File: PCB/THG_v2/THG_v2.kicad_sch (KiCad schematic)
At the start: 9 parts, among them J1 AM2315_Conn, J2 Conn_01x04_Male, J3 Conn_01x04_Male, J4 Conn_01x06_Male, J5 Screw_Terminal_01x02, U1 mini_esp32

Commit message: adding previous gerber file
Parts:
- added R3: n/a, Resistor_THT:R_Axial_DIN0207_L6.3mm_D2.5mm_P10.16mm_Horizontal, symbol Device:R
- added S1: DTS-6, Lib_Kicad:DTS-6, symbol DTS-6:DTS-6
- J2: value Conn_01x04_Male -> LCD_conn
- J3: value Conn_01x04_Male -> RTC_Conn
- J4: value Conn_01x06_Male -> SD_card_conn
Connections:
- net +5V: now also S1.3
- net GND: now also U1.1 (GND), U1.22 (GND), U1.33 (GND), R3.1, S1.2
- new net: R3.2, S1.1

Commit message: adding pcb pic
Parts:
- J5: value Screw_Terminal_01x02 -> AC_in_terminal
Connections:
- net +5V: now also R1.1, R2.1
- net SCL: now also J1.4 (Pin_4)
- net SDA: now also J1.3 (Pin_3)
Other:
- moved on the sheet: J5, R1, R2

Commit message: rev
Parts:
- removed J1: AM2315_Conn, Connector_JST:JST_EH_B4B-EH-A_1x04_P2.50mm_Vertical, symbol Connector:Conn_01x04_Male
- added J1: AM2315_Jack, Lib_Kicad:TRRS-PJ-320A, symbol Connector:AudioJack3_Ground
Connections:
- net +5V: now also J1.T
- net GND: now also J1.G
- net SCL: now also J1.S
- net SDA: now also J1.R
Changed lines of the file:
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@@
-    (stroke (width 0) (type default) (color 0 0 0 0))
-  )
-  (wire (pts (xy 95.25 138.43) (xy 95.25 128.27))
-    (stroke (width 0) (type default) (color 0 0 0 0))
-  )
-  (wire (pts (xy 95.25 121.92) (xy 95.25 125.73))
     (stroke (width 0) (type default) (color 0 0 0 0))
   )
@@
     (stroke (width 0) (type default) (color 0 0 0 0))
   )
+  (wire (pts (xy 86.36 128.27) (xy 99.06 128.27))
+    (stroke (width 0) (type default) (color 0 0 0 0))
+  )
   (wire (pts (xy 215.9 129.54) (xy 212.09 129.54))
     (stroke (width 0) (type default) (color 0 0 0 0))
   )
-  (wire (pts (xy 74.93 133.35) (xy 72.39 133.35))
+  (wire (pts (xy 88.9 123.19) (xy 86.36 123.19))
     (stroke (width 0) (type default) (color 0 0 0 0))
   )
@@
     (stroke (width 0) (type default) (color 0 0 0 0))
   )
-  (wire (pts (xy 74.93 130.81) (xy 72.39 130.81))
+  (wire (pts (xy 88.9 125.73) (xy 86.36 125.73))
     (stroke (width 0) (type default) (color 0 0 0 0))
   )
@@
     (stroke (width 0) (type default) (color 0 0 0 0))
   )
-  (wire (pts (xy 95.25 128.27) (xy 72.39 128.27))
-    (stroke (width 0) (type default) (color 0 0 0 0))
-  )
   (wire (pts (xy 198.12 62.23) (xy 200.66 62.23))
     (stroke (width 0) (type default) (color 0 0 0 0))
@@
     (stroke (width 0) (type default) (color 0 0 0 0))
   )
+  (wire (pts (xy 99.06 128.27) (xy 99.06 120.65))
+    (stroke (width 0) (type default) (color 0 0 0 0))
+  )
   (wire (pts (xy 99.06 93.98) (xy 96.52 93.98))
-    (stroke (width 0) (type default) (color 0 0 0 0))
-  )
-  (wire (pts (xy 95.25 125.73) (xy 72.39 125.73))
     (stroke (width 0) (type default) (color 0 0 0 0))
   )
@@
     )
   )
-  (global_label "SDA" (shape input) (at 74.93 130.81 0) (fields_autoplaced)
+  (global_label "SDA" (shape input) (at 88.9 125.73 0) (fields_autoplaced)
     (effects (font (size 1.27 1.27)) (justify left))
-    (property "Intersheet References" "${INTERSHEET_REFS}" (id 0) (at 80.9112 130.7306 0)
+    (property "Intersheet References" "${INTERSHEET_REFS}" (id 0) (at 94.8812 125.8094 0)
       (effects (font (size 1.27 1.27)) (justify left) hide)
     )
@@
     )
   )
-  (global_label "SCL" (shape input) (at 74.93 133.35 0) (fields_autoplaced)
+  (global_label "SCL" (shape input) (at 88.9 123.19 0) (fields_autoplaced)
     (effects (font (size 1.27 1.27)) (justify left))
-    (property "Intersheet References" "${INTERSHEET_REFS}" (id 0) (at 80.8507 133.2706 0)
+    (property "Intersheet References" "${INTERSHEET_REFS}" (id 0) (at 94.8207 123.2694 0)
       (effects (font (size 1.27 1.27)) (justify left) hide)
     )
@@
     (pin "1")
   )
-  (symbol (lib_id "Connector:Conn_01x04_Male") (at 67.31 128.27 0) (unit 1)
-    (in_bom yes) (on_board yes) (fields_autoplaced)
-    (property "Reference" "J1" (id 0) (at 67.945 120.65 0))
-    (property "Value" "AM2315_Conn" (id 1) (at 67.945 123.19 0))
-    (property "Footprint" "Connector_JST:JST_EH_B4B-EH-A_1x04_P2.50mm_Vertical" (id 2) (at 67.31 128.27 0)
-      (effects (font (size 1.27 1.27)) hide)
-    )
-    (property "Datasheet" "~" (id 3) (at 67.31 128.27 0)
-      (effects (font (size 1.27 1.27)) hide)
-    )
-    (pin "1")
-    (pin "2")
-    (pin "3")
-    (pin "4")
+  (symbol (lib_id "Connector:AudioJack3_Ground") (at 81.28 125.73 0) (unit 1)
+    (in_bom yes) (on_board yes) (fields_autoplaced)
+    (property "Reference" "J1" (id 0) (at 79.375 116.84 0))
+    (property "Value" "AM2315_Jack" (id 1) (at 79.375 119.38 0))
+    (property "Footprint" "Lib_Kicad:TRRS-PJ-320A" (id 2) (at 81.28 125.73 0)
+      (effects (font (size 1.27 1.27)) hide)
+    )
+    (property "Datasheet" "~" (id 3) (at 81.28 125.73 0)
+      (effects (font (size 1.27 1.27)) hide)
+    )
+    (pin "G")
+    (pin "R")
+    (pin "S")
+    (pin "T")
   )
   (symbol (lib_id "DTS-6:DTS-6") (at 207.01 129.54 270) (unit 1)
@@
     (pin "1")
   )
-  (symbol (lib_id "power:+5V") (at 95.25 121.92 0) (unit 1)
-    (in_bom yes) (on_board yes) (fields_autoplaced)
-    (property "Reference" "#PWR0105" (id 0) (at 95.25 125.73 0)
-      (effects (font (size 1.27 1.27)) hide)
-    )
-    (property "Value" "+5V" (id 1) (at 95.25 116.84 0))
-    (property "Footprint" "" (id 2) (at 95.25 121.92 0)
-      (effects (font (size 1.27 1.27)) hide)
-    )
-    (property "Datasheet" "" (id 3) (at 95.25 121.92 0)
+  (symbol (lib_id "power:+5V") (at 99.06 120.65 0) (mirror y) (unit 1)
+    (in_bom yes) (on_board yes) (fields_autoplaced)
+    (property "Reference" "#PWR0105" (id 0) (at 99.06 124.46 0)
+      (effects (font (size 1.27 1.27)) hide)
+    )
+    (property "Value" "+5V" (id 1) (at 99.06 115.57 0))
+    (property "Footprint" "" (id 2) (at 99.06 120.65 0)
+      (effects (font (size 1.27 1.27)) hide)
+    )
+    (property "Datasheet" "" (id 3) (at 99.06 120.65 0)
       (effects (font (size 1.27 1.27)) hide)
     )
@@
   (symbol (lib_id "power:+5V") (at 119.38 142.24 0) (unit 1)
     (in_bom yes) (on_board yes) (fields_autoplaced)
-    (property "Reference" "#PWR?" (id 0) (at 119.38 146.05 0)
+    (property "Reference" "#PWR0116" (id 0) (at 119.38 146.05 0)
       (effects (font (size 1.27 1.27)) hide)
     )
@@
     (pin "1")
   )
-  (symbol (lib_id "power:GND") (at 95.25 138.43 0) (unit 1)
-    (in_bom yes) (on_board yes) (fields_autoplaced)
-    (property "Reference" "#PWR0106" (id 0) (at 95.25 144.78 0)
-      (effects (font (size 1.27 1.27)) hide)
-    )
-    (property "Value" "GND" (id 1) (at 95.25 143.51 0))
-    (property "Footprint" "" (id 2) (at 95.25 138.43 0)
-      (effects (font (size 1.27 1.27)) hide)
-    )
-    (property "Datasheet" "" (id 3) (at 95.25 138.43 0)
+  (symbol (lib_id "power:GND") (at 81.28 133.35 0) (unit 1)
+    (in_bom yes) (on_board yes) (fields_autoplaced)
+    (property "Reference" "#PWR0106" (id 0) (at 81.28 139.7 0)
+      (effects (font (size 1.27 1.27)) hide)
+    )
+    (property "Value" "GND" (id 1) (at 81.28 138.43 0))
+    (property "Footprint" "" (id 2) (at 81.28 133.35 0)
+      (effects (font (size 1.27 1.27)) hide)
+    )
+    (property "Datasheet" "" (id 3) (at 81.28 133.35 0)
       (effects (font (size 1.27 1.27)) hide)
     )
@@
     )
     (path "/50c1423a-2336-485b-a1eb-eea3967751f9"
-      (reference "#PWR?") (unit 1) (value "+5V") (footprint "")
-    )
-    (path "/27d7923d-62c0-4fe7-8bd6-2b6190754bc6"
-      (reference "J1") (unit 1) (value "AM2315_Conn") (footprint "Connector_JST:JST_EH_B4B-EH-A_1x04_P2.50mm_Vertical")
+      (reference "#PWR0116") (unit 1) (value "+5V") (footprint "")
+    )
+    (path "/1e362064-1c5c-469c-8576-28390879d190"
+      (reference "J1") (unit 1) (value "AM2315_Jack") (footprint "Lib_Kicad:TRRS-PJ-320A")
     )
     (path "/eacfccdb-496f-4d23-be5f-1e7301d4a980"

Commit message: revisi
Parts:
- added H1, H2, H3: MountingHole_Pad, MountingHole:MountingHole_2.2mm_M2_Pad_Via, symbol Mechanical:MountingHole_Pad
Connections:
- net GND: now also H1.1, H2.1, H3.1
- no-connect marks 0 -> 29
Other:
- note added: "Button"
- note added: "Connectors"
- note added: "Microcontroller Board"
- note added: "Mounting Pads"
- note added: "Power Supply"
- moved on the sheet: J1, J2, J3, J4, J5, PS1, R1, R2, R3, S1, U1

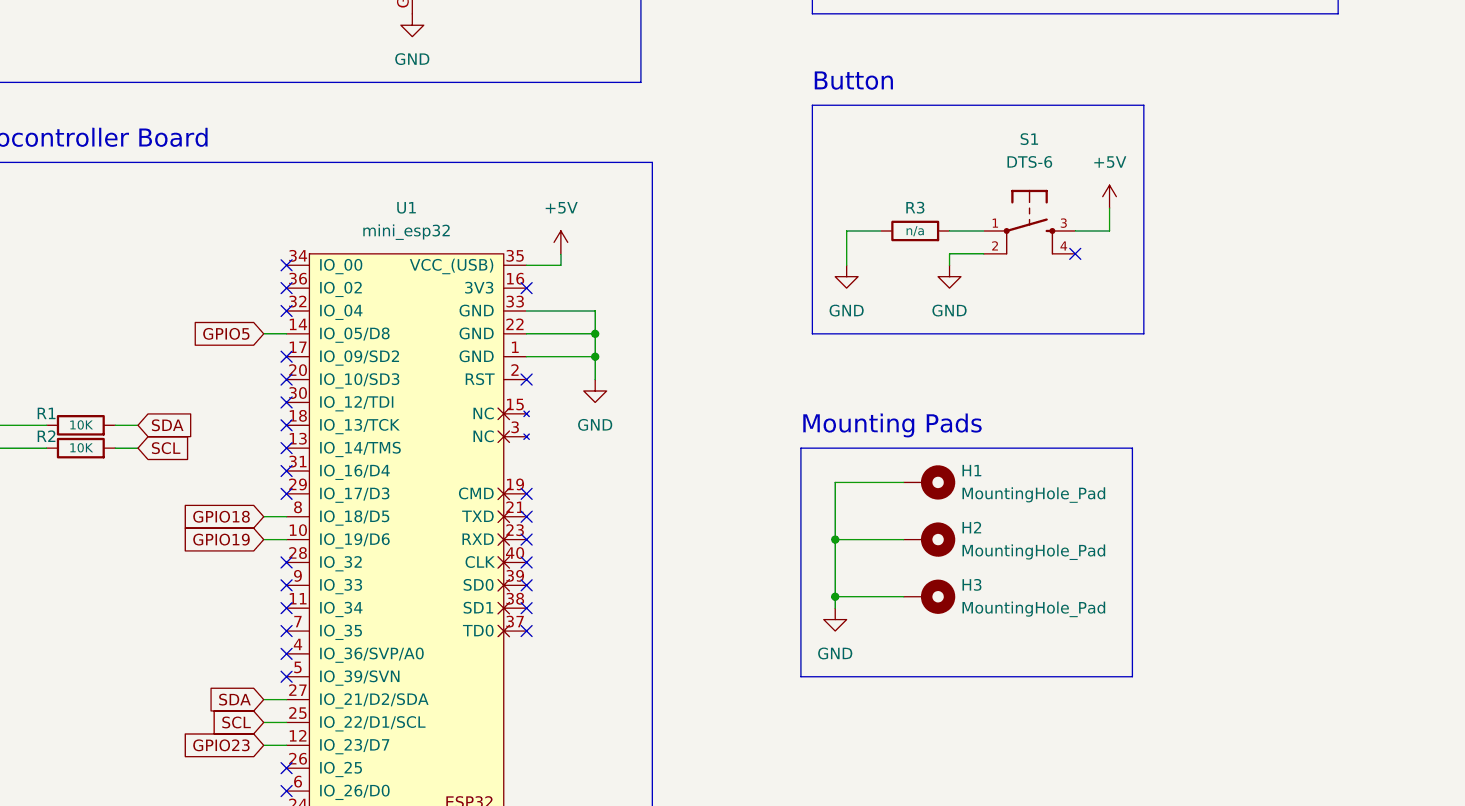
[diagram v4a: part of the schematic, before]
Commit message: revisi tata letak dan rangkaian button
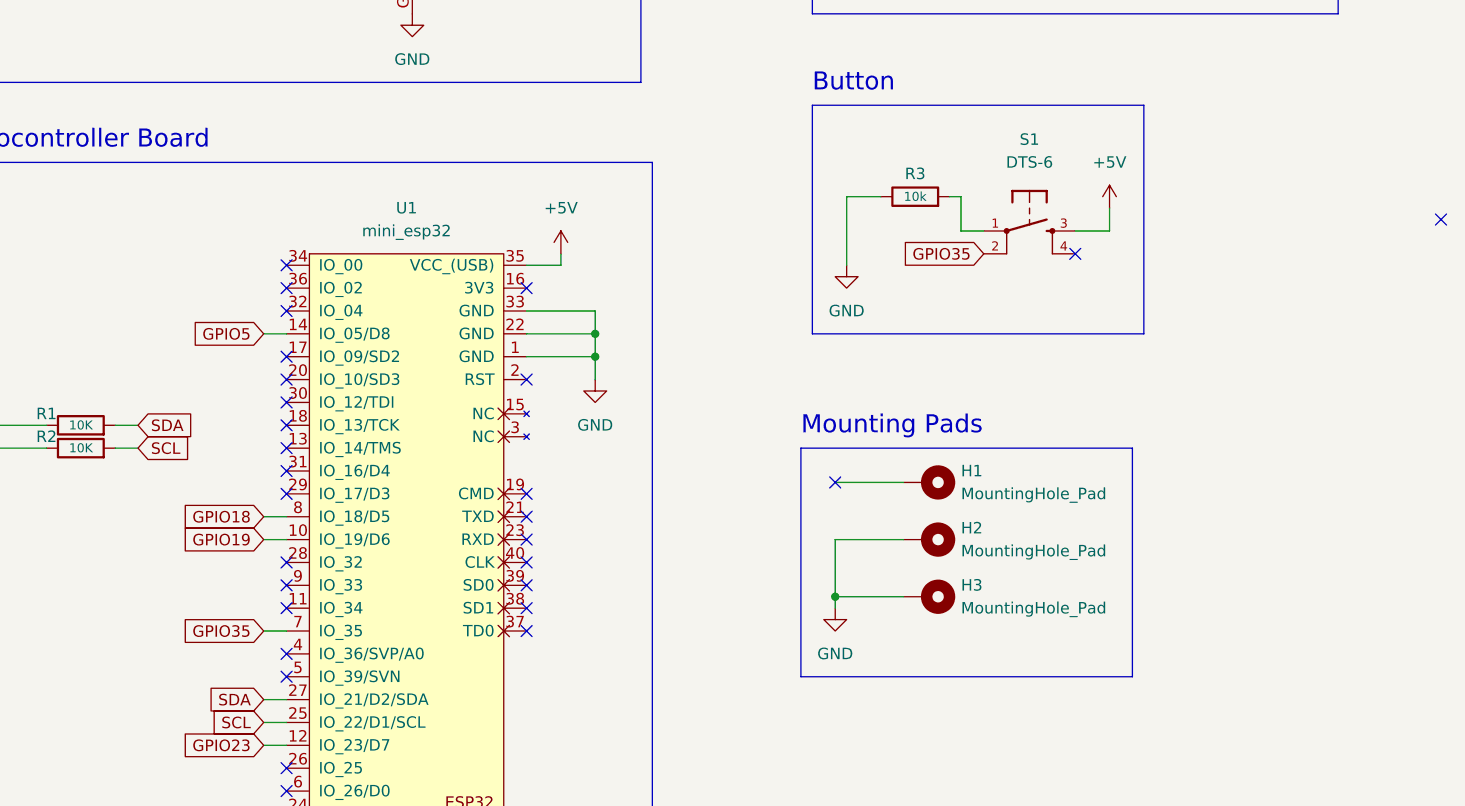
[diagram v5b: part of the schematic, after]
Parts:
- R3: value n/a -> 10k
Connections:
- net GND: no longer H1.1, S1.2
- net GPIO35: now reaches U1.7 (IO_35)
- net GPIO35: now also S1.2
- no-connect marks 29 -> 30
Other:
- moved on the sheet: R3
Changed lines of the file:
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@@
   (junction (at 140.97 123.19) (diameter 0) (color 0 0 0 0)
-  )
-  (junction (at 167.64 143.51) (diameter 0) (color 0 0 0 0)
   )
   (no_connect (at 106.68 168.91))
@@
   (no_connect (at 106.68 151.13))
   (no_connect (at 106.68 158.75))
-  (no_connect (at 106.68 153.67))
   (no_connect (at 106.68 128.27))
   (no_connect (at 133.35 143.51))
@@
   (no_connect (at 106.68 133.35))
   (no_connect (at 106.68 125.73))
+  (no_connect (at 167.64 137.16))
+  (no_connect (at 234.95 107.95))
   (no_connect (at 194.31 111.76))
+  (wire (pts (xy 168.91 105.41) (xy 172.72 105.41))
+    (stroke (width 0) (type default) (color 0 0 0 0))
+  )
   (polyline (pts (xy 201.93 95.25) (xy 201.93 120.65))
     (stroke (width 0) (type default) (color 0 0 0 0))
@@
     (stroke (width 0) (type default) (color 0 0 0 0))
   )
+  (wire (pts (xy 104.14 153.67) (xy 106.68 153.67))
+    (stroke (width 0) (type default) (color 0 0 0 0))
+  )
   (wire (pts (xy 137.16 113.03) (xy 133.35 113.03))
     (stroke (width 0) (type default) (color 0 0 0 0))
@@
     (stroke (width 0) (type default) (color 0 0 0 0))
   )
+  (wire (pts (xy 181.61 109.22) (xy 184.15 109.22))
+    (stroke (width 0) (type default) (color 0 0 0 0))
+  )
   (wire (pts (xy 170.18 68.58) (xy 170.18 69.85))
     (stroke (width 0) (type default) (color 0 0 0 0))
@@
     (stroke (width 0) (type default) (color 0 0 0 0))
   )
-  (wire (pts (xy 168.91 109.22) (xy 172.72 109.22))
-    (stroke (width 0) (type default) (color 0 0 0 0))
-  )
   (wire (pts (xy 85.09 41.91) (xy 82.55 41.91))
     (stroke (width 0) (type default) (color 0 0 0 0))
@@
     (stroke (width 0) (type default) (color 0 0 0 0))
   )
-  (wire (pts (xy 167.64 143.51) (xy 167.64 137.16))
-    (stroke (width 0) (type default) (color 0 0 0 0))
-  )
   (wire (pts (xy 72.39 127) (xy 72.39 130.81))
     (stroke (width 0) (type default) (color 0 0 0 0))
   )
-  (wire (pts (xy 184.15 109.22) (xy 180.34 109.22))
-    (stroke (width 0) (type default) (color 0 0 0 0))
-  )
   (wire (pts (xy 170.18 69.85) (xy 173.99 69.85))
     (stroke (width 0) (type default) (color 0 0 0 0))
@@
     (stroke (width 0) (type default) (color 0 0 0 0))
   )
-  (wire (pts (xy 168.91 109.22) (xy 168.91 113.03))
-    (stroke (width 0) (type default) (color 0 0 0 0))
-  )
-  (wire (pts (xy 180.34 111.76) (xy 180.34 113.03))
+  (wire (pts (xy 168.91 105.41) (xy 168.91 113.03))
     (stroke (width 0) (type default) (color 0 0 0 0))
   )
@@
     (stroke (width 0) (type default) (color 0 0 0 0))
   )
+  (wire (pts (xy 180.34 105.41) (xy 181.61 105.41))
+    (stroke (width 0) (type default) (color 0 0 0 0))
+  )
   (wire (pts (xy 90.17 130.81) (xy 87.63 130.81))
     (stroke (width 0) (type default) (color 0 0 0 0))
   )
+  (wire (pts (xy 181.61 105.41) (xy 181.61 109.22))
+    (stroke (width 0) (type default) (color 0 0 0 0))
+  )
   (wire (pts (xy 128.27 41.91) (xy 125.73 41.91))
     (stroke (width 0) (type default) (color 0 0 0 0))
   )
   (wire (pts (xy 137.16 49.53) (xy 125.73 49.53))
-    (stroke (width 0) (type default) (color 0 0 0 0))
-  )
-  (wire (pts (xy 184.15 111.76) (xy 180.34 111.76))
     (stroke (width 0) (type default) (color 0 0 0 0))
   )
@@
   (text "Mounting Pads" (at 163.83 132.08 0)
     (effects (font (size 2 2)) (justify left bottom))
+  )
+  (global_label "GPIO35" (shape input) (at 104.14 153.67 180) (fields_autoplaced)
+    (effects (font (size 1.27 1.27)) (justify right))
+    (property "Intersheet References" "${INTERSHEET_REFS}" (id 0) (at 94.8326 153.5906 0)
+      (effects (font (size 1.27 1.27)) (justify right) hide)
+    )
   )
   (global_label "SCL" (shape input) (at 85.09 74.93 0) (fields_autoplaced)
@@
     )
   )
+  (global_label "GPIO35" (shape input) (at 184.15 111.76 180) (fields_autoplaced)
+    (effects (font (size 1.27 1.27)) (justify right))
+    (property "Intersheet References" "${INTERSHEET_REFS}" (id 0) (at 174.8426 111.6806 0)
+      (effects (font (size 1.27 1.27)) (justify right) hide)
+    )
+  )
   (global_label "SDA" (shape input) (at 104.14 161.29 180) (fields_autoplaced)
     (effects (font (size 1.27 1.27)) (justify right))
@@
     (pin "3")
     (pin "4")
-  )
-  (symbol (lib_id "power:GND") (at 180.34 113.03 0) (unit 1)
-    (in_bom yes) (on_board yes) (fields_autoplaced)
-    (property "Reference" "#PWR0114" (id 0) (at 180.34 119.38 0)
-      (effects (font (size 1.27 1.27)) hide)
-    )
-    (property "Value" "GND" (id 1) (at 180.34 118.11 0))
-    (property "Footprint" "" (id 2) (at 180.34 113.03 0)
-      (effects (font (size 1.27 1.27)) hide)
-    )
-    (property "Datasheet" "" (id 3) (at 180.34 113.03 0)
-      (effects (font (size 1.27 1.27)) hide)
-    )
-    (pin "1")
   )
   (symbol (lib_id "power:+5V") (at 138.43 72.39 0) (mirror y) (unit 1)
@@
     (pin "1")
   )
-  (symbol (lib_id "Device:R") (at 176.53 109.22 90) (unit 1)
+  (symbol (lib_id "Device:R") (at 176.53 105.41 90) (unit 1)
     (in_bom yes) (on_board yes)
-    (property "Reference" "R3" (id 0) (at 176.53 106.68 90))
-    (property "Value" "n/a" (id 1) (at 176.53 109.22 90)
+    (property "Reference" "R3" (id 0) (at 176.53 102.87 90))
+    (property "Value" "10k" (id 1) (at 176.53 105.41 90)
       (effects (font (size 1 1)))
     )
-    (property "Footprint" "Resistor_THT:R_Axial_DIN0207_L6.3mm_D2.5mm_P10.16mm_Horizontal" (id 2) (at 176.53 110.998 90)
-      (effects (font (size 1.27 1.27)) hide)
-    )
-    (property "Datasheet" "~" (id 3) (at 176.53 109.22 0)
+    (property "Footprint" "Resistor_THT:R_Axial_DIN0207_L6.3mm_D2.5mm_P10.16mm_Horizontal" (id 2) (at 176.53 107.188 90)
+      (effects (font (size 1.27 1.27)) hide)
+    )
+    (property "Datasheet" "~" (id 3) (at 176.53 105.41 0)
       (effects (font (size 1.27 1.27)) hide)
     )
@@
       (reference "#PWR0113") (unit 1) (value "GND") (footprint "")
     )
-    (path "/308793dc-e057-47da-a29e-df7cc3a6659f"
-      (reference "#PWR0114") (unit 1) (value "GND") (footprint "")
-    )
     (path "/bc9d52b2-c70a-4768-b78c-5dcb5a0ddf2f"
       (reference "#PWR0115") (unit 1) (value "+5V") (footprint "")
@@
     )
     (path "/6df354e5-0ed8-486f-aaba-922f1d8df851"
-      (reference "R3") (unit 1) (value "n/a") (footprint "Resistor_THT:R_Axial_DIN0207_L6.3mm_D2.5mm_P10.16mm_Horizontal")
+      (reference "R3") (unit 1) (value "10k") (footprint "Resistor_THT:R_Axial_DIN0207_L6.3mm_D2.5mm_P10.16mm_Horizontal")
     )
     (path "/2eea6c0b-d8ad-476f-8416-4a43347c3306"
